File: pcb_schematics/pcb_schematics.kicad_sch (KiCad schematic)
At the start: 73 parts, among them J1 CUE_SJ1-352XNG, J2 Conn_01x01_Pin, J3 Conn_01x05, J4 Conn_01x05, J5 Conn_01x05, SW1 SW_Push, U1 RPi_Pico_TH, U2 RDA5807M_Module, U3 LM386, U4 LM386

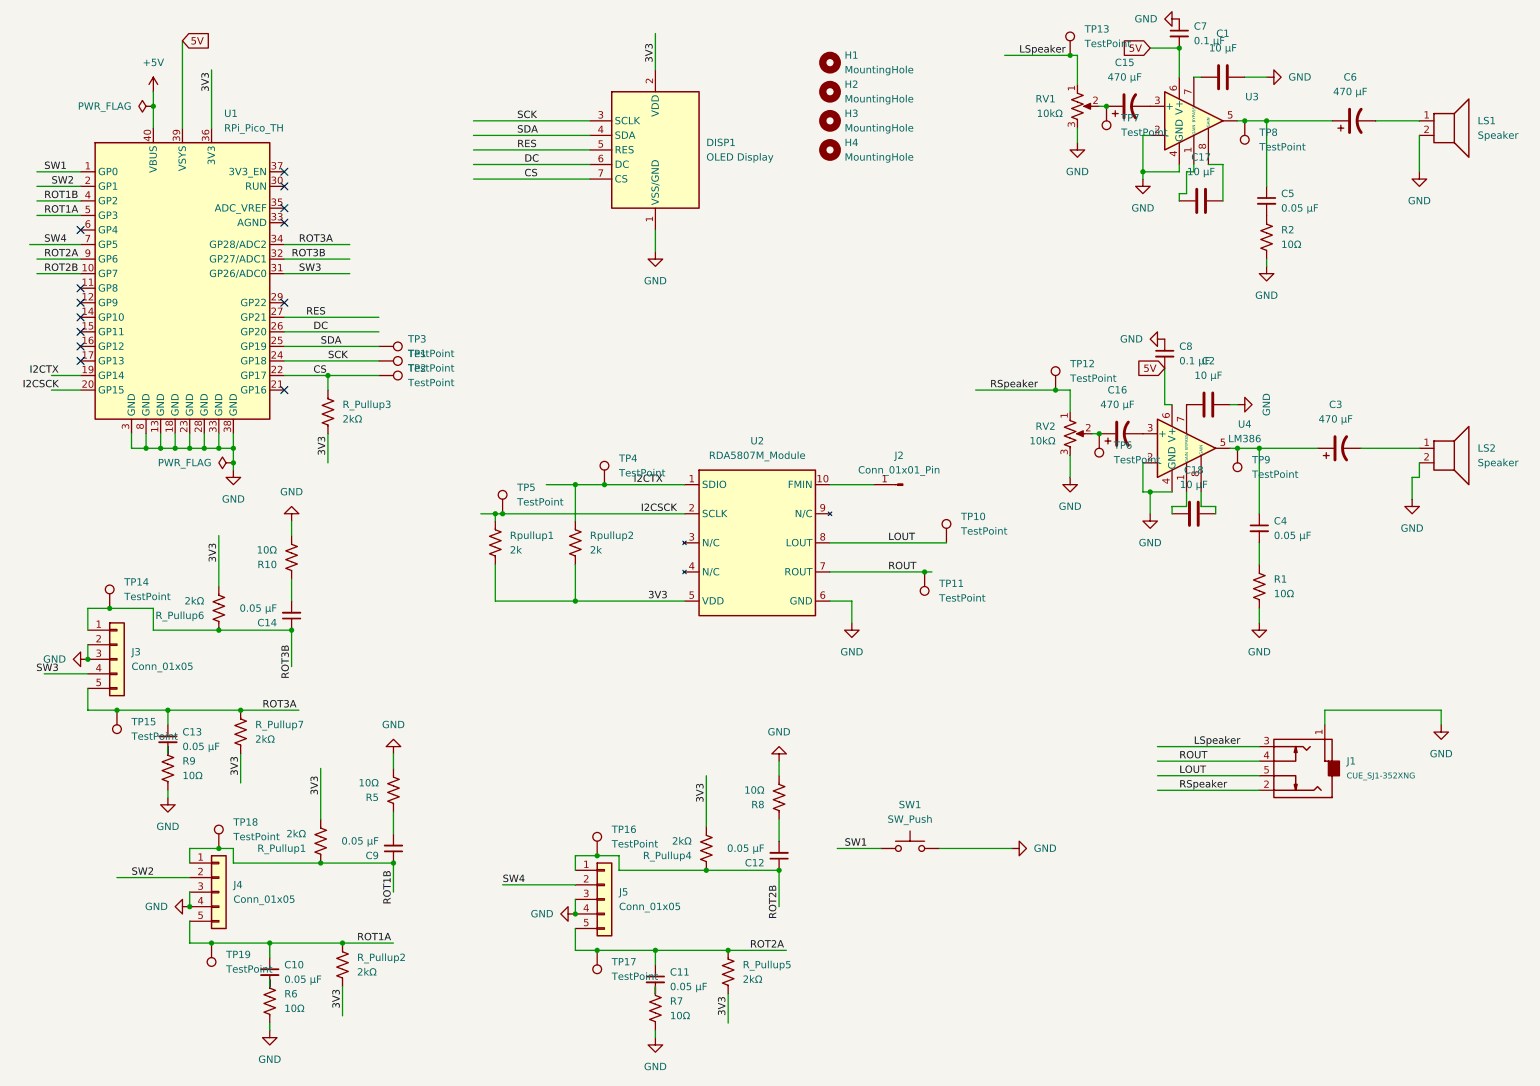
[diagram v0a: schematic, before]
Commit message: Revision 3
Changed the amplifier and the rotary encoder schemtic. Needs work on pcb
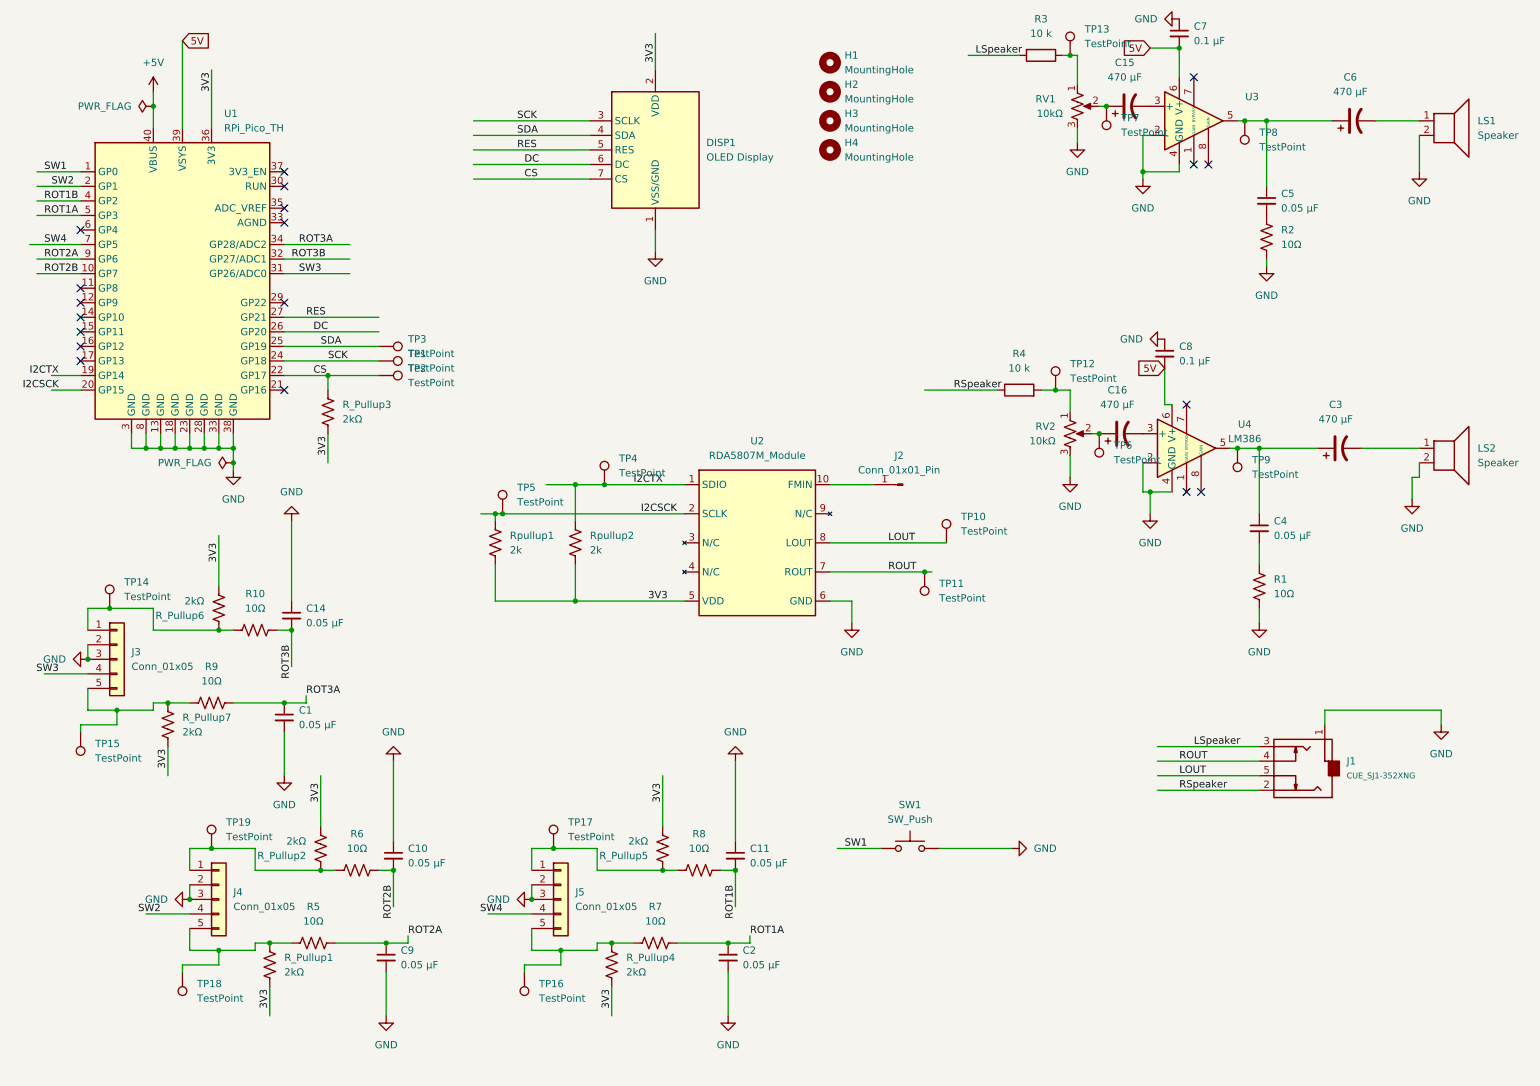
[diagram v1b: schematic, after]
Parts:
- removed C1, C17, C18, C2: 10 µF, Capacitor_THT:CP_Radial_D6.3mm_P2.50mm, symbol Device:C
- removed C12, C13: 0.05 µF, Capacitor_THT:C_Axial_L3.8mm_D2.6mm_P7.50mm_Horizontal, symbol Device:C_Small
- added C1, C2: 0.05 µF, Capacitor_THT:C_Axial_L3.8mm_D2.6mm_P7.50mm_Horizontal, symbol Device:C_Small
- added R3, R4: 10 k, symbol Device:R
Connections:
- net GND: now also C10.1, C11.1, C14.1, C9.2, J4.2 (Pin_2), J5.2 (Pin_2), C1.2, C2.2; no longer J4.4 (Pin_4), J5.4 (Pin_4), R10.2, R5.2, R6.2, R7.2, R8.2, R9.2
- net LSpeaker: now also R3.2; no longer RV1.1, TP13.1
- net ROT1A: now also R7.2, C2.1; no longer C10.1, J4.5 (Pin_5), R_Pullup2.1, TP19.1
- net ROT1B: now also C11.2, R8.1; no longer C9.1, J4.1 (Pin_1), R_Pullup1.1, TP18.1
- net ROT2A: now also C9.1, R5.2; no longer C11.1, J5.5 (Pin_5), R_Pullup5.1, TP17.1
- net ROT2B: now also C10.2, R6.1; no longer J5.1 (Pin_1), R_Pullup4.1, TP16.1
- net ROT3A: now also R9.2, C1.1; no longer J3.5 (Pin_5), R_Pullup7.1, TP15.1
- net ROT3B: now also C14.2, R10.1; no longer C14.1, J3.1 (Pin_1), R_Pullup6.1, TP14.1
- net RSpeaker: now also R4.1; no longer RV2.1, TP12.1
- net SW2: now also J4.4 (Pin_4); no longer J4.2 (Pin_2)
- net SW4: now also J5.4 (Pin_4); no longer J5.2 (Pin_2)
- net at R5.1: now also J4.5 (Pin_5), R_Pullup1.1, TP18.1; no longer C9.2
- net at R9.1: now also J3.5 (Pin_5), R_Pullup7.1, TP15.1
- net at R7.1: now also J5.5 (Pin_5), R_Pullup4.1, TP16.1; no longer C11.2
- new net: R3.1, RV1.1, TP13.1
- new net: J3.1 (Pin_1), R10.2, R_Pullup6.1, TP14.1
- new net: R4.2, RV2.1, TP12.1
- new net: J4.1 (Pin_1), R6.2, R_Pullup2.1, TP19.1
- new net: J5.1 (Pin_1), R8.2, R_Pullup5.1, TP17.1
- no-connect marks 13 -> 19
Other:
- moved on the sheet: C14, TP15

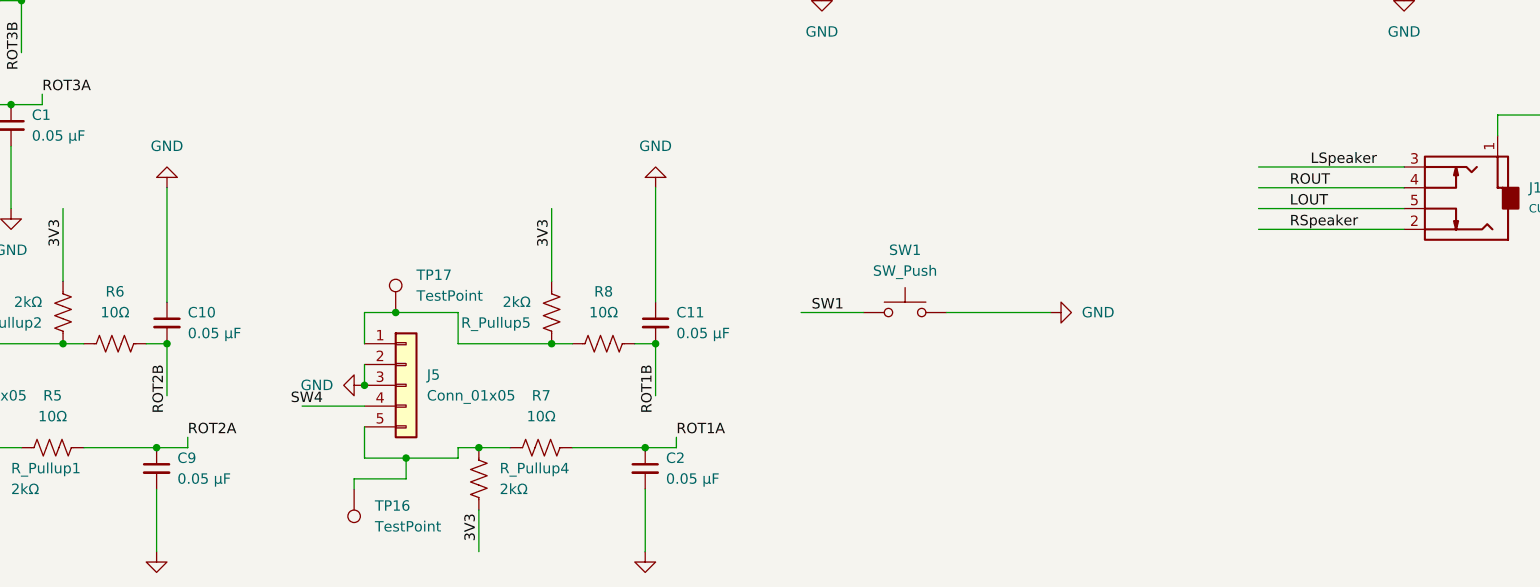
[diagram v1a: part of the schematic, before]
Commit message: completes third version of PCB
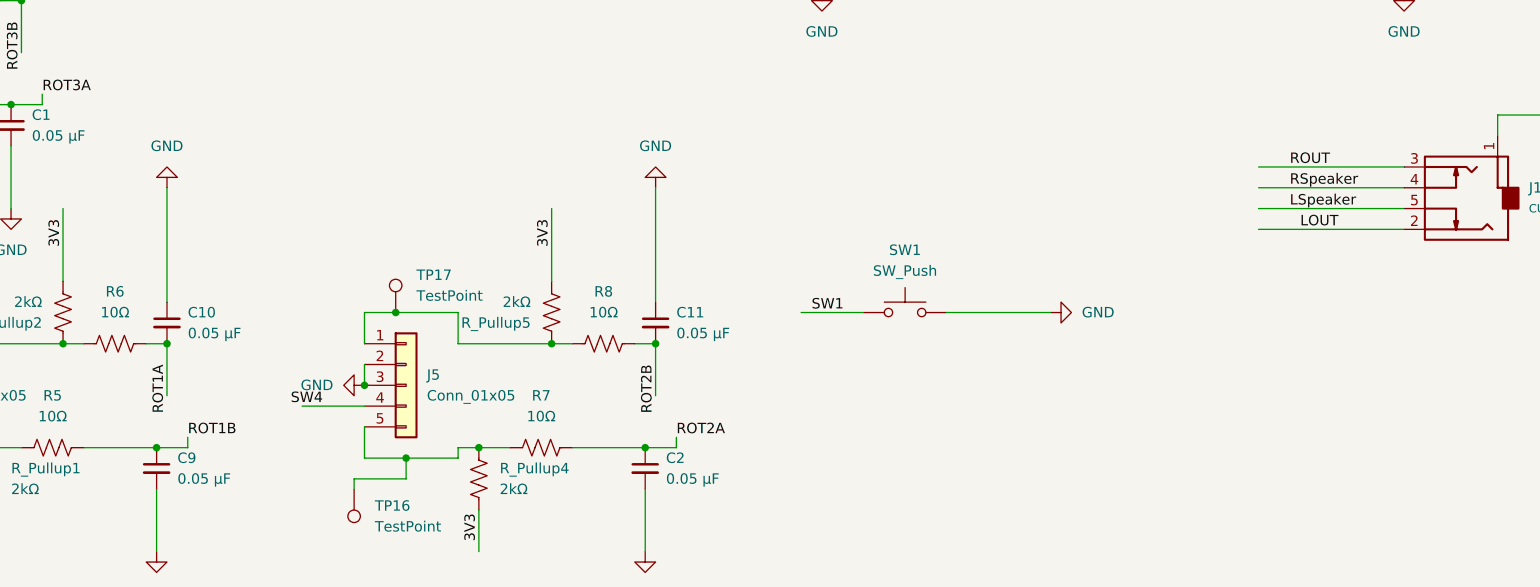
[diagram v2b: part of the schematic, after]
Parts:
- R3, R4: footprint (none) -> Resistor_THT:R_Axial_DIN0207_L6.3mm_D2.5mm_P10.16mm_Horizontal
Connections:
- net LOUT: now also J1.2 (Tip); no longer J1.5 (Ring_Switch)
- net LSpeaker: now also J1.5 (Ring_Switch); no longer J1.3 (Tip)
- net ROT1A: now also C10.2, R6.1; no longer C2.1, R7.2
- net ROT1B: now also C9.1, R5.2; no longer C11.2, R8.1
- net ROT2A: now also C2.1, R7.2; no longer C9.1, R5.2
- net ROT2B: now also C11.2, R8.1; no longer C10.2, R6.1
- net ROUT: now also J1.3 (Tip); no longer J1.4 (Tip_Switch)
- net RSpeaker: now also J1.4 (Tip_Switch); no longer J1.2 (Tip)
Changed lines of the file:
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@@
     (effects (font (size 1.27 1.27)) (justify right bottom))
   )
-  (label "ROT1B" (at 142.24 165.1 270) (fields_autoplaced)
+  (label "ROT2B" (at 142.24 165.1 270) (fields_autoplaced)
     (effects (font (size 1.27 1.27)) (justify right bottom))
   )
@@
     (effects (font (size 1.27 1.27)) (justify left bottom))
   )
-  (label "LSpeaker" (at 222.25 140.97 0) (fields_autoplaced)
-    (effects (font (size 1.27 1.27)) (justify left bottom))
-  )
-  (label "ROT2B" (at 82.55 165.1 270) (fields_autoplaced)
+  (label "LSpeaker" (at 219.71 146.05 0) (fields_autoplaced)
+    (effects (font (size 1.27 1.27)) (justify left bottom))
+  )
+  (label "ROT1A" (at 82.55 165.1 270) (fields_autoplaced)
     (effects (font (size 1.27 1.27)) (justify right bottom))
   )
-  (label "ROT1A" (at 144.78 173.99 0) (fields_autoplaced)
+  (label "ROT2A" (at 144.78 173.99 0) (fields_autoplaced)
     (effects (font (size 1.27 1.27)) (justify left bottom))
   )
@@
     (effects (font (size 1.27 1.27)) (justify left bottom))
   )
+  (label "LOUT" (at 220.98 148.59 0) (fields_autoplaced)
+    (effects (font (size 1.27 1.27)) (justify left bottom))
+  )
   (label "CS" (at 68.58 76.2 0) (fields_autoplaced)
     (effects (font (size 1.27 1.27)) (justify left bottom))
@@
   )
   (label "I2CTX" (at 124.46 95.25 0) (fields_autoplaced)
-    (effects (font (size 1.27 1.27)) (justify left bottom))
-  )
-  (label "LOUT" (at 219.71 146.05 0) (fields_autoplaced)
     (effects (font (size 1.27 1.27)) (justify left bottom))
   )
@@
     (effects (font (size 1.27 1.27)) (justify right bottom))
   )
-  (label "ROT2A" (at 85.09 173.99 0) (fields_autoplaced)
+  (label "ROT1B" (at 85.09 173.99 0) (fields_autoplaced)
     (effects (font (size 1.27 1.27)) (justify left bottom))
   )
@@
     (effects (font (size 1.27 1.27)) (justify left bottom))
   )
-  (label "ROUT" (at 219.71 143.51 0) (fields_autoplaced)
-    (effects (font (size 1.27 1.27)) (justify left bottom))
-  )
   (label "3V3" (at 69.85 147.32 270) (fields_autoplaced)
     (effects (font (size 1.27 1.27)) (justify right bottom))
   )
+  (label "ROUT" (at 219.71 140.97 0) (fields_autoplaced)
+    (effects (font (size 1.27 1.27)) (justify left bottom))
+  )
   (label "3V3" (at 71.12 90.17 90) (fields_autoplaced)
     (effects (font (size 1.27 1.27)) (justify left bottom))
@@
     (effects (font (size 1.27 1.27)) (justify right bottom))
   )
-  (label "RSpeaker" (at 219.71 148.59 0) (fields_autoplaced)
+  (label "RSpeaker" (at 219.71 143.51 0) (fields_autoplaced)
     (effects (font (size 1.27 1.27)) (justify left bottom))
   )
@@
       (effects (font (size 1.27 1.27)))
     )
-    (property "Footprint" "" (at 191.77 80.518 90)
+    (property "Footprint" "Resistor_THT:R_Axial_DIN0207_L6.3mm_D2.5mm_P10.16mm_Horizontal" (at 191.77 80.518 90)
       (effects (font (size 1.27 1.27)) hide)
     )
@@
       (effects (font (size 1.27 1.27)))
     )
-    (property "Footprint" "" (at 195.58 18.542 90)
-      (effects (font (size 1.27 1.27)) hide)
-    )
+    (property "Footprint" "Resistor_THT:R_Axial_DIN0207_L6.3mm_D2.5mm_P10.16mm_Horizontal" (at 195.58 18.542 90)
+      (effects (font (size 1.27 1.27)) hide)
+    )
